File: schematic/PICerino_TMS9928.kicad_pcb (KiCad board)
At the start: 2 copper layers, 101.7 x 106.9 mm, 45 parts, among them CON1 PICERINO-EDGE, J1 Conn_01x02, J2 Conn_01x02, J3 Conn_01x02, J4 Conn_01x02, Y1 Crystal

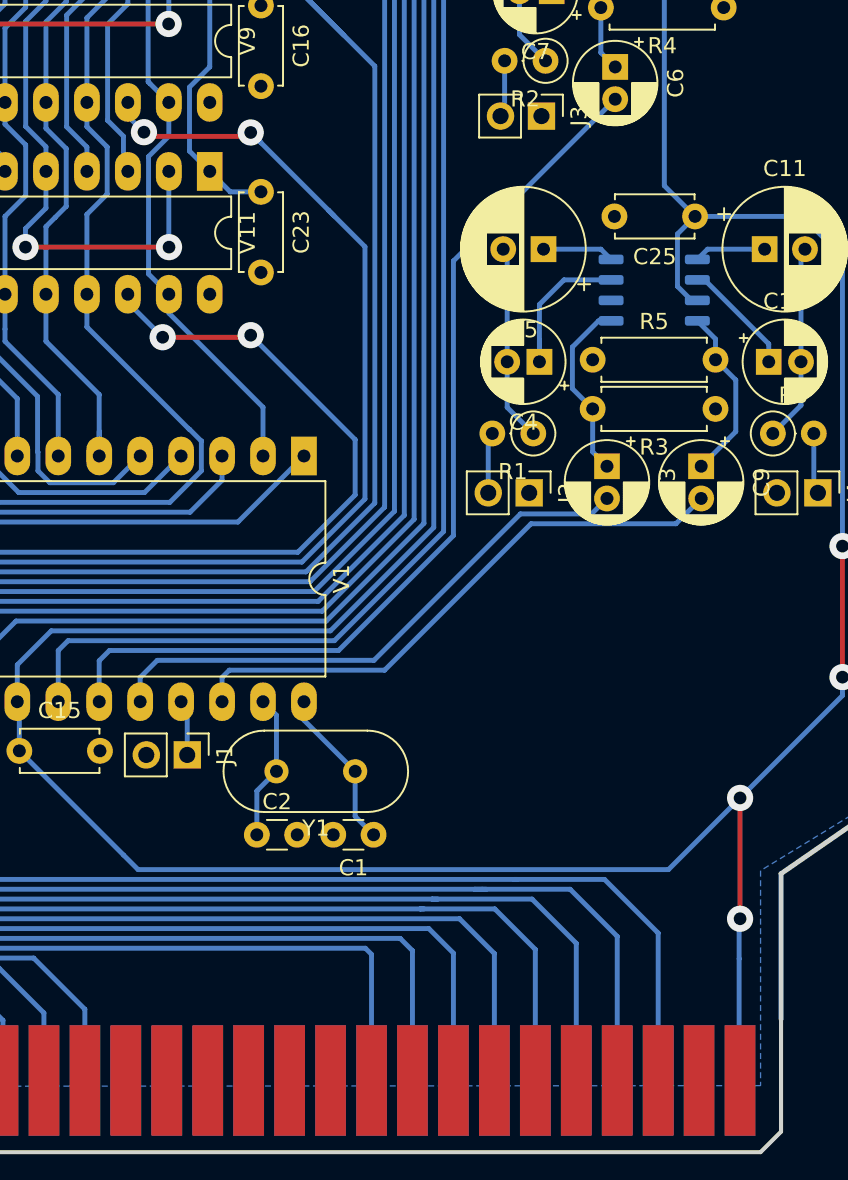
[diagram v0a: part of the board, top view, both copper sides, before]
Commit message: added 470 ohm load resistors to output of VDP pre TI spec (whoops)
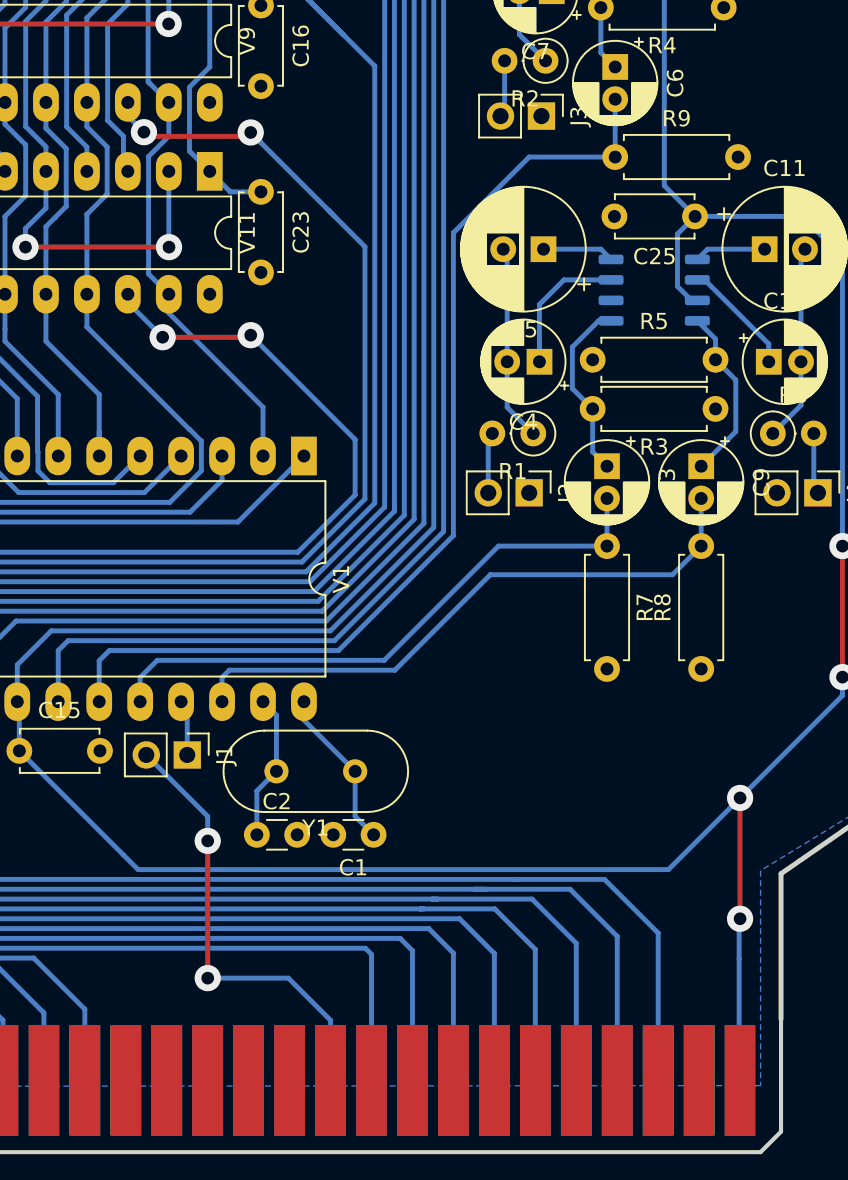
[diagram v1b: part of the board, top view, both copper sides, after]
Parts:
- added R7: 470R, Resistor_THT:R_Axial_DIN0207_L6.3mm_D2.5mm_P7.62mm_Horizontal, F.Cu at (185.0, 116.7)
- added R8: 470R, Resistor_THT:R_Axial_DIN0207_L6.3mm_D2.5mm_P7.62mm_Horizontal, F.Cu at (190.9, 124.3)
- added R9: 470R, Resistor_THT:R_Axial_DIN0207_L6.3mm_D2.5mm_P7.62mm_Horizontal, F.Cu at (185.5, 92.6)
- J2: value Conn_01x02 -> Y_Conn_01x02
- J3: value Conn_01x02 -> BY_Conn_01x02
- J4: value Conn_01x02 -> RY_Conn_01x02
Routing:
- net VSS: track 0.00 -> 27.9 mm, vias 0 -> 2
- net /Yb: track 59.0 -> 62.1 mm
- net /Yr: track 35.8 -> 37.6 mm
- net /Y: track 35.1 -> 36.8 mm

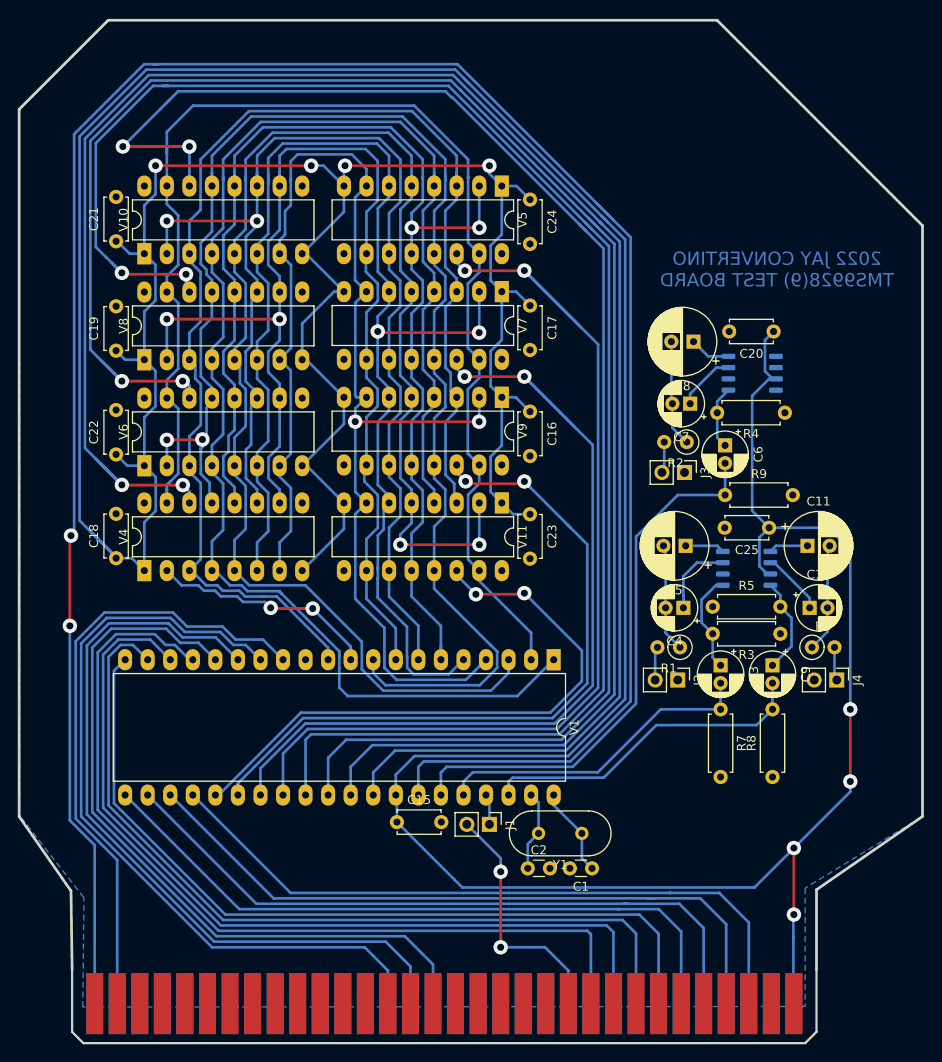
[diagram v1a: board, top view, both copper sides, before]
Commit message: updated schematic with new features. 1) test points for dram testing. 2) jumpers to route video output signals for testing.
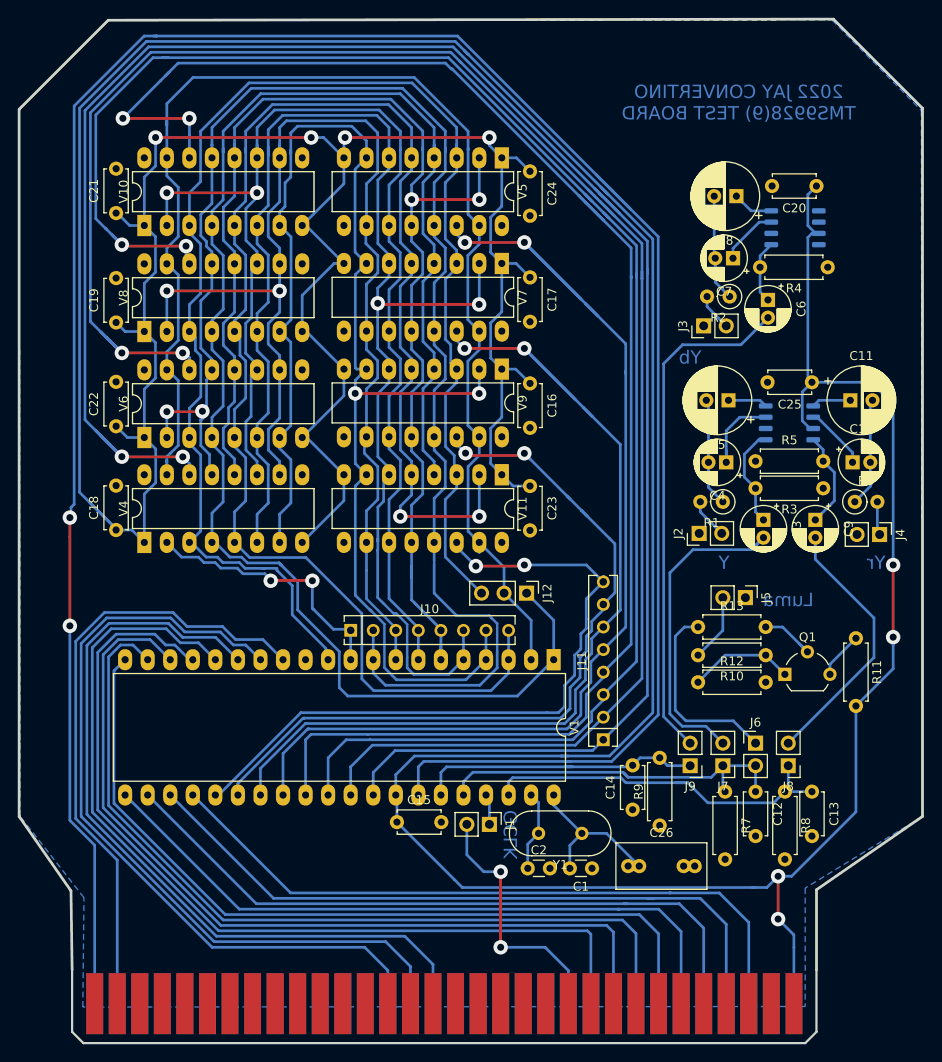
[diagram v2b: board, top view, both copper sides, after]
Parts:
- added C12: 100nF, Capacitor_THT:C_Disc_D4.7mm_W2.5mm_P5.00mm, F.Cu at (189.0, 126.0)
- added C13: 100nF, Capacitor_THT:C_Disc_D4.7mm_W2.5mm_P5.00mm, F.Cu at (195.3, 126.0)
- added C14: 100nF, Capacitor_THT:C_Disc_D4.7mm_W2.5mm_P5.00mm, F.Cu at (175.1, 128.0)
- added C26: 20pf, Capacitor_THT:C_Rect_L10.0mm_W5.0mm_P5.00mm_P7.50mm, F.Cu at (174.6, 134.4)
- added J10: Conn_01x08, Package_SIP:SIP-8_19x3mm_P2.54mm, F.Cu at (143.4, 107.8)
- added J11: Conn_01x08, Package_SIP:SIP-8_19x3mm_P2.54mm, F.Cu at (171.8, 120.1)
- added J12: Conn_01x03, Connector_PinHeader_2.54mm:PinHeader_1x03_P2.54mm_Vertical, F.Cu at (163.2, 103.6)
- added J5: Y_Conn_01x02, Connector_PinHeader_2.54mm:PinHeader_1x02_P2.54mm_Vertical, F.Cu at (187.8, 104.1)
- added J6: Conn_01x02, Connector_PinHeader_2.54mm:PinHeader_1x02_P2.54mm_Vertical, F.Cu at (189.0, 120.5)
- added J7: Conn_01x02, Connector_PinHeader_2.54mm:PinHeader_1x02_P2.54mm_Vertical, F.Cu at (185.3, 123.1)
- added J8: Conn_01x02, Connector_PinHeader_2.54mm:PinHeader_1x02_P2.54mm_Vertical, F.Cu at (192.7, 123.1)
- added J9: Conn_01x02, Connector_PinHeader_2.54mm:PinHeader_1x02_P2.54mm_Vertical, F.Cu at (181.6, 123.1)
- added Q1: 2N3904, Package_TO_SOT_THT:TO-92_Wide, F.Cu at (192.3, 112.8)
- added R10: 27R, Resistor_THT:R_Axial_DIN0207_L6.3mm_D2.5mm_P7.62mm_Horizontal, F.Cu at (190.1, 110.6)
- added R11: 10R, Resistor_THT:R_Axial_DIN0207_L6.3mm_D2.5mm_P7.62mm_Horizontal, F.Cu at (200.3, 108.7)
- added R12: 580R, Resistor_THT:R_Axial_DIN0207_L6.3mm_D2.5mm_P7.62mm_Horizontal, F.Cu at (182.5, 113.7)
- added R13: 470R, Resistor_THT:R_Axial_DIN0207_L6.3mm_D2.5mm_P7.62mm_Horizontal, F.Cu at (182.5, 107.4)
- C1: value 22pF -> 18pF
- C2: value 22pF -> 33pF
- moved R9 37.9 mm to (178.2, 129.8), turned to 90 degrees
- moved C3 17.1 mm to (189.9, 95.4)
- moved C20 17.1 mm to (195.8, 57.8)
- moved C25 17.1 mm to (195.3, 79.9)
- moved C6 17.1 mm to (190.4, 70.6)
- moved C7 17.1 mm to (186.4, 65.9)
- moved C8 17.1 mm to (186.8, 58.9)
- moved C9 17.1 mm to (195.7, 95.4)
- moved R2 17.1 mm to (186.1, 70.2)
- moved R5 17.1 mm to (189.0, 88.8)
- moved R4 17.1 mm to (197.1, 66.9)
- moved V2 17.1 mm to (192.8, 84.5)
- moved V3 17.1 mm to (193.4, 62.5)
- moved C10 17.1 mm to (199.9, 88.9)
- moved C11 17.1 mm to (199.6, 81.9)
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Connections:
- C1 pad 1: Net-(C1-Pad1) -> VSS
- C1 pad 2: VSS -> Net-(C1-Pad2)
- C3 pad 2: /Y -> Net-(C3-Pad2)
- C6 pad 2: /Yb -> Net-(C6-Pad2)
- C9 pad 2: /Yr -> Net-(C9-Pad2)
- R8 pad 1: VSS -> /Yr
- R8 pad 2: /Yr -> VSS
- R9 pad 1: /Yb -> VSS
- R9 pad 2: VSS -> /Yb
- V1 pad 40: Net-(C1-Pad1) -> Net-(C1-Pad2)
- Y1 pad 1: Net-(C1-Pad1) -> Net-(C1-Pad2)
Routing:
- net Net-(C6-Pad2): track 0.00 -> 57.9 mm
- net Net-(C3-Pad2): track 0.00 -> 35.8 mm
- net Net-(C9-Pad2): track 0.00 -> 29.9 mm
- net /Yb: track 62.1 -> 32.7 mm
- net VCC: track 580.1 -> 607.0 mm
- net Net-(J6-Pad1): track 0.00 -> 21.9 mm
- net Net-(C1-Pad2): track 0.00 -> 19.4 mm
- net /RnW: track 149.5 -> 168.3 mm
- net /nRESET: track 258.8 -> 274.6 mm
- net Net-(Q1-Pad1): track 0.00 -> 12.5 mm
- net /R0: track 214.1 -> 226.1 mm
- net /nRAS: track 169.3 -> 180.9 mm
- net /R7: track 68.3 -> 78.7 mm
- net Net-(C1-Pad1): track 10.0 -> 0.00 mm
- net /R1: track 203.9 -> 213.5 mm
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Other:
- board size 101.7 x 106.9 mm -> 101.7 x 107.1 mm
- board text added: "GCLK"
- board text added: "Luma"
- board text added: "Y"
- board text added: "Yb"
- board text added: "Yr"

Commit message: schematic fix, 100nF cap is way too high a value and filters and the backporch of the signal (blurs it). 220pF is the value from a few TI example schematics. Works great, clear picture
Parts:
- C12, C13, C14: value 100nF -> 220pf

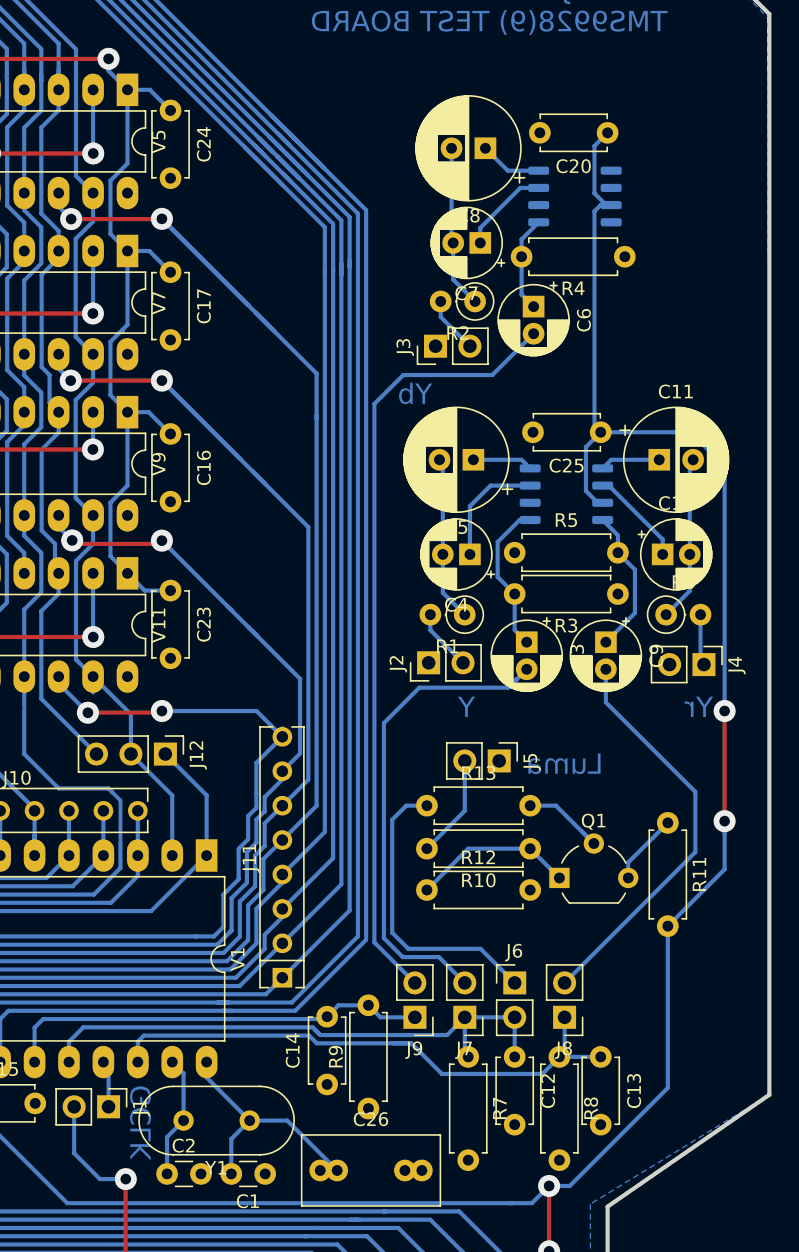
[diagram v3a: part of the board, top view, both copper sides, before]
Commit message: removed luma circuit, no need. added 75ohm voltage divider per the 2267 data sheet. do not populate for 6db increase, other wise use it for most applications.
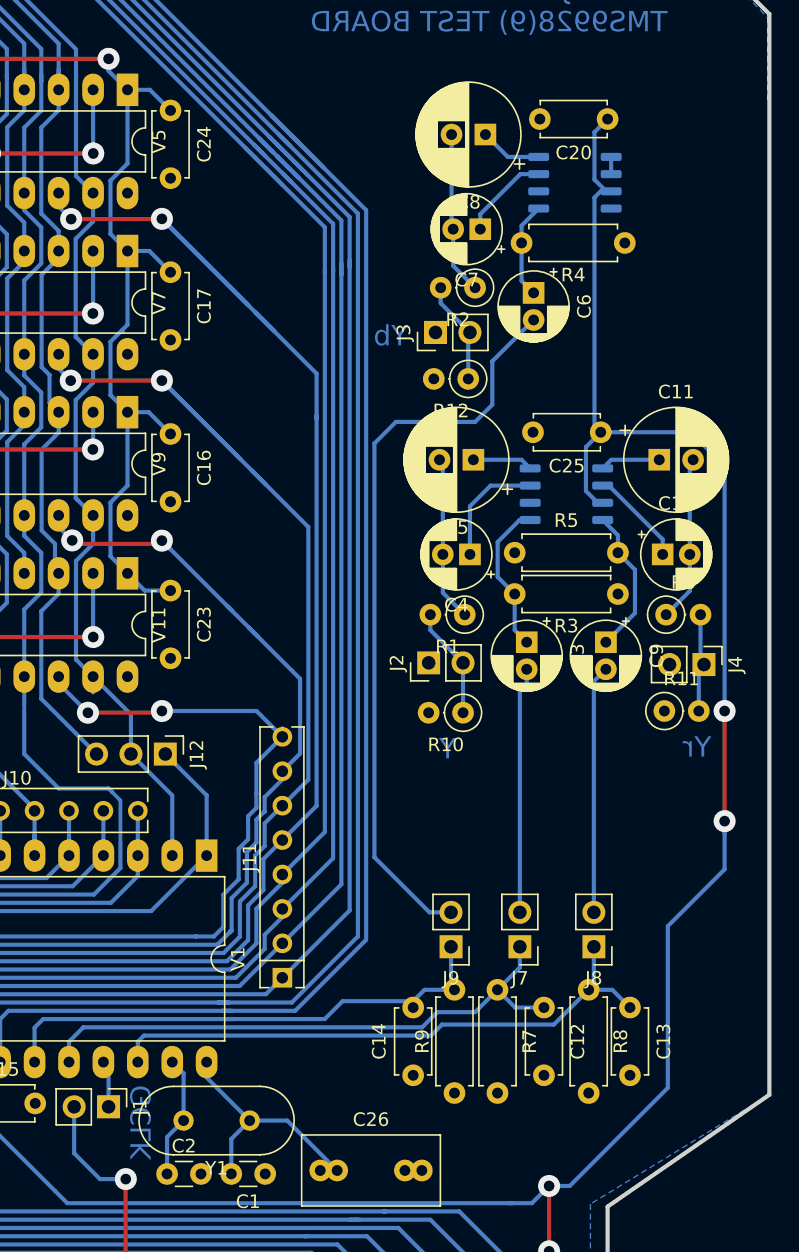
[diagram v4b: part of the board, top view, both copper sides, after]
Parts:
- removed J5: Y_Conn_01x02, Connector_PinHeader_2.54mm:PinHeader_1x02_P2.54mm_Vertical
- removed J6: Conn_01x02, Connector_PinHeader_2.54mm:PinHeader_1x02_P2.54mm_Vertical
- removed Q1: 2N3904, Package_TO_SOT_THT:TO-92_Wide
- removed R13: 470R, Resistor_THT:R_Axial_DIN0207_L6.3mm_D2.5mm_P7.62mm_Horizontal
- R10: value 27R -> 75R; footprint Resistor_THT:R_Axial_DIN0207_L6.3mm_D2.5mm_P7.62mm_Horizontal -> Resistor_THT:R_Axial_DIN0207_L6.3mm_D2.5mm_P2.54mm_Vertical
- R11: value 10R -> 75R; footprint Resistor_THT:R_Axial_DIN0207_L6.3mm_D2.5mm_P7.62mm_Horizontal -> Resistor_THT:R_Axial_DIN0207_L6.3mm_D2.5mm_P2.54mm_Vertical
- R12: value 580R -> 75R; footprint Resistor_THT:R_Axial_DIN0207_L6.3mm_D2.5mm_P7.62mm_Horizontal -> Resistor_THT:R_Axial_DIN0207_L6.3mm_D2.5mm_P2.54mm_Vertical
- moved R12 37.8 mm to (185.5, 75.9), turned to 180 degrees
- moved R10 11.2 mm to (185.2, 100.6)
- moved R11 8.26 mm to (200.0, 100.5), turned to 0 degrees
- moved J7 6.61 mm to (189.4, 117.9)
- moved R9 6.45 mm to (184.5, 128.7)
- moved C14 6.39 mm to (181.5, 127.3)
- moved J9 5.85 mm to (184.3, 117.9)
- moved J8 5.64 mm to (194.8, 117.9)
- moved R8 5.40 mm to (194.4, 121.0)
- moved R7 5.40 mm to (187.7, 121.0)
- moved C13 4.23 mm to (197.5, 122.3)
- moved C12 4.23 mm to (191.1, 122.3)
- moved J3 1.02 mm to (183.1, 72.5)
- moved R4 1.02 mm to (197.1, 65.9)
- moved C20 1.02 mm to (195.8, 56.8)
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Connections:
- R10 pad 1: Net-(Q1-Pad1) -> Net-(J2-Pad2)
- R11 pad 1: Net-(Q1-Pad3) -> VSS
- R11 pad 2: VCC -> Net-(J4-Pad1)
- R12 pad 1: Net-(Q1-Pad1) -> Net-(J3-Pad2)
- V3 pad 6: Net-(V3-Pad6) -> Net-(V3-Pad5)
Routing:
- net Net-(J6-Pad1): track 21.9 -> 0.00 mm
- net Net-(C3-Pad2): track 35.8 -> 18.1 mm
- net Net-(Q1-Pad1): track 12.5 -> 0.00 mm
- net Net-(C9-Pad2): track 29.9 -> 18.3 mm
- net Net-(R10-Pad2): track 7.63 -> 0.00 mm
- net Net-(Q1-Pad2): track 7.10 -> 0.00 mm
- net /Yb: track 32.7 -> 38.8 mm
- net Net-(Q1-Pad3): track 5.27 -> 0.00 mm
- net Net-(J2-Pad2): track 4.91 -> 8.60 mm
- net Net-(J4-Pad1): track 3.79 -> 7.38 mm
- net Net-(J3-Pad2): track 4.20 -> 7.68 mm
- net Net-(C6-Pad2): track 57.9 -> 55.3 mm
- net Net-(V3-Pad5): track 0.00 -> 1.27 mm
- net /Yr: track 42.0 -> 43.0 mm
- net VCC: track 607.0 -> 608.0 mm
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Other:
- board text removed: "Luma"
